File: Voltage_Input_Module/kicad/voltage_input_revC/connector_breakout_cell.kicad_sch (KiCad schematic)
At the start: 2 parts, among them J2 T4143012041-000, J3 Conn_01x02

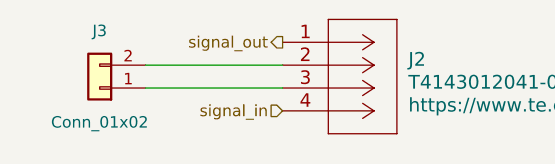
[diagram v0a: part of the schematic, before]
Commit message: Untangled birds nest. Laid out footprints for PCB. Added ground connection to connector breakout cell. Need to make traces, making sure they're wide enough.
Co-Authored-By: Andrew-Matteson136382 <67286784+Andrew-Matteson136382@users.noreply.github.com>
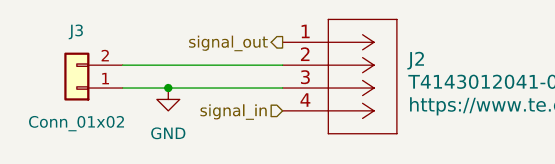
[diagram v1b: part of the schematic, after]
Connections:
- net GND: now reaches J2.3, J3.1 (Pin_1)
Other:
- moved on the sheet: J3
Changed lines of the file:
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@@
 (kicad_sch (version 20230121) (generator eeschema)
   (paper "A4")
-  (wire (pts (xy 87.63 67.31) (xy 102.87 67.31))
+  (junction (at 90.17 69.85) (diameter 0) (color 0 0 0 0)
+  )
+  (wire (pts (xy 90.17 69.85) (xy 102.87 69.85))
     (stroke (width 0) (type default))
   )
-  (wire (pts (xy 87.63 69.85) (xy 102.87 69.85))
+  (wire (pts (xy 85.09 67.31) (xy 102.87 67.31))
+    (stroke (width 0) (type default))
+  )
+  (wire (pts (xy 85.09 69.85) (xy 90.17 69.85))
     (stroke (width 0) (type default))
   )
@@
     (effects (font (size 1.27 1.27)) (justify right))
   )
-  (symbol (lib_id "Connector_Generic:Conn_01x02") (at 82.55 69.85 180) (unit 1)
-    (in_bom yes) (on_board yes) (dnp no)
-    (property "Reference" "J3" (at 82.55 63.5 0)
+  (symbol (lib_id "power:GND") (at 90.17 69.85 0) (unit 1)
+    (in_bom yes) (on_board yes) (dnp no) (fields_autoplaced)
+    (property "Reference" "#PWR06" (at 90.17 76.2 0)
+      (effects (font (size 1.27 1.27)) hide)
+    )
+    (property "Value" "GND" (at 90.17 74.93 0)
       (effects (font (size 1.27 1.27)))
     )
-    (property "Value" "Conn_01x02" (at 82.55 73.66 0)
+    (property "Footprint" "" (at 90.17 69.85 0)
+      (effects (font (size 1.27 1.27)) hide)
+    )
+    (property "Datasheet" "" (at 90.17 69.85 0)
+      (effects (font (size 1.27 1.27)) hide)
+    )
+    (pin "1")
+    (instances
+      (project "voltage_input_revC"
+        (path "/8ce21293-ec61-4589-b6e0-775962e481c9/5bd90b5b-1f53-4b9d-b91a-0ecab666451e"
+          (reference "#PWR06") (unit 1)
+        )
+        (path "/8ce21293-ec61-4589-b6e0-775962e481c9/bd1d19e9-0237-4310-aaea-5d450cc02d92"
+          (reference "#PWR03") (unit 1)
+        )
+        (path "/8ce21293-ec61-4589-b6e0-775962e481c9/3b431700-c16b-497e-b9ab-7f8185822b5f"
+          (reference "#PWR04") (unit 1)
+        )
+        (path "/8ce21293-ec61-4589-b6e0-775962e481c9/3fea3b95-37b3-4ed6-9f3e-2331c43b9fb1"
+          (reference "#PWR05") (unit 1)
+        )
+        (path "/8ce21293-ec61-4589-b6e0-775962e481c9/59167fe4-672b-45c1-b7a3-8b21369d1ffd"
+          (reference "#PWR07") (unit 1)
+        )
+        (path "/8ce21293-ec61-4589-b6e0-775962e481c9/d88549a4-fd82-4df1-9371-996172e29850"
+          (reference "#PWR08") (unit 1)
+        )
+        (path "/8ce21293-ec61-4589-b6e0-775962e481c9/4540e8c2-e254-48ea-b049-6ae43f8634ec"
+          (reference "#PWR09") (unit 1)
+        )
+        (path "/8ce21293-ec61-4589-b6e0-775962e481c9/80f0acbd-6f33-43ea-bfb2-f1839874f5b2"
+          (reference "#PWR010") (unit 1)
+        )
+        (path "/8ce21293-ec61-4589-b6e0-775962e481c9/25ff17b7-e299-4e85-a406-e78403fe26df"
+          (reference "#PWR011") (unit 1)
+        )
+        (path "/8ce21293-ec61-4589-b6e0-775962e481c9/d00f4568-5e3d-4163-891a-be0fa40adfb8"
+          (reference "#PWR012") (unit 1)
+        )
+        (path "/8ce21293-ec61-4589-b6e0-775962e481c9/e3827e04-1489-4cf9-a060-8b0fb256f85b"
+          (reference "#PWR013") (unit 1)
+        )
+        (path "/8ce21293-ec61-4589-b6e0-775962e481c9/b5e24955-f0bf-4f24-b245-15d7650dd48d"
+          (reference "#PWR014") (unit 1)
+        )
+        (path "/8ce21293-ec61-4589-b6e0-775962e481c9/e547ac3d-f28c-4dc2-81b9-c0386aaaaff2"
+          (reference "#PWR015") (unit 1)
+        )
+        (path "/8ce21293-ec61-4589-b6e0-775962e481c9/4fbbbb42-8e46-4186-b7ae-25728c1d55ed"
+          (reference "#PWR016") (unit 1)
+        )
+        (path "/8ce21293-ec61-4589-b6e0-775962e481c9/3dc67075-e378-44da-8d7e-d78d9036b1e0"
+          (reference "#PWR017") (unit 1)
+        )
+        (path "/8ce21293-ec61-4589-b6e0-775962e481c9/c000c5ef-6766-456b-9e1b-e732133e48cc"
+          (reference "#PWR018") (unit 1)
+        )
+      )
+    )
+  )
+  (symbol (lib_id "Connector_Generic:Conn_01x02") (at 80.01 69.85 180) (unit 1)
+    (in_bom yes) (on_board yes) (dnp no)
+    (property "Reference" "J3" (at 80.01 63.5 0)
       (effects (font (size 1.27 1.27)))
     )
-    (property "Footprint" "custom_libraries:powerpole-1545-2x1" (at 82.55 69.85 0)
+    (property "Value" "Conn_01x02" (at 80.01 73.66 0)
+      (effects (font (size 1.27 1.27)))
+    )
+    (property "Footprint" "custom_libraries:powerpole-1545-2x1" (at 80.01 69.85 0)
       (effects (font (size 1.27 1.27)) hide)
     )
-    (property "Datasheet" "~" (at 82.55 69.85 0)
+    (property "Datasheet" "~" (at 80.01 69.85 0)
       (effects (font (size 1.27 1.27)) hide)
     )

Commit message: Finished traces, Implemented footprints and 3d models for powerpole connections. Added mounting holes and edge cuts. Need to implement silk screen callouts for sensors.
Co-Authored-By: Andrew-Matteson136382 <67286784+Andrew-Matteson136382@users.noreply.github.com>
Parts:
- J3: footprint custom_libraries:powerpole-1545-2x1 -> MRDT_Connectors:Square_Anderson_2_V_Side_By_Side
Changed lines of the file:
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@@
       (effects (font (size 1.27 1.27)))
     )
-    (property "Footprint" "custom_libraries:powerpole-1545-2x1" (at 80.01 69.85 0)
+    (property "Footprint" "MRDT_Connectors:Square_Anderson_2_V_Side_By_Side" (at 80.01 69.85 0)
       (effects (font (size 1.27 1.27)) hide)
     )
